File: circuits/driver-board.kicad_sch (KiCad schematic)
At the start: 72 parts, among them J1 Conn_01x18_Female, J2 USB4120-03-C_REVA, J3 Motor_Conn_01x04, J4 Screw_Terminals, J5 Conn_01x06_Female, Q1 SS8050-G, Q2 SS8050-G, SW1 RST_SW_Push, U1 CP2102N-Axx-xQFN24, U2 BA33DD0T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

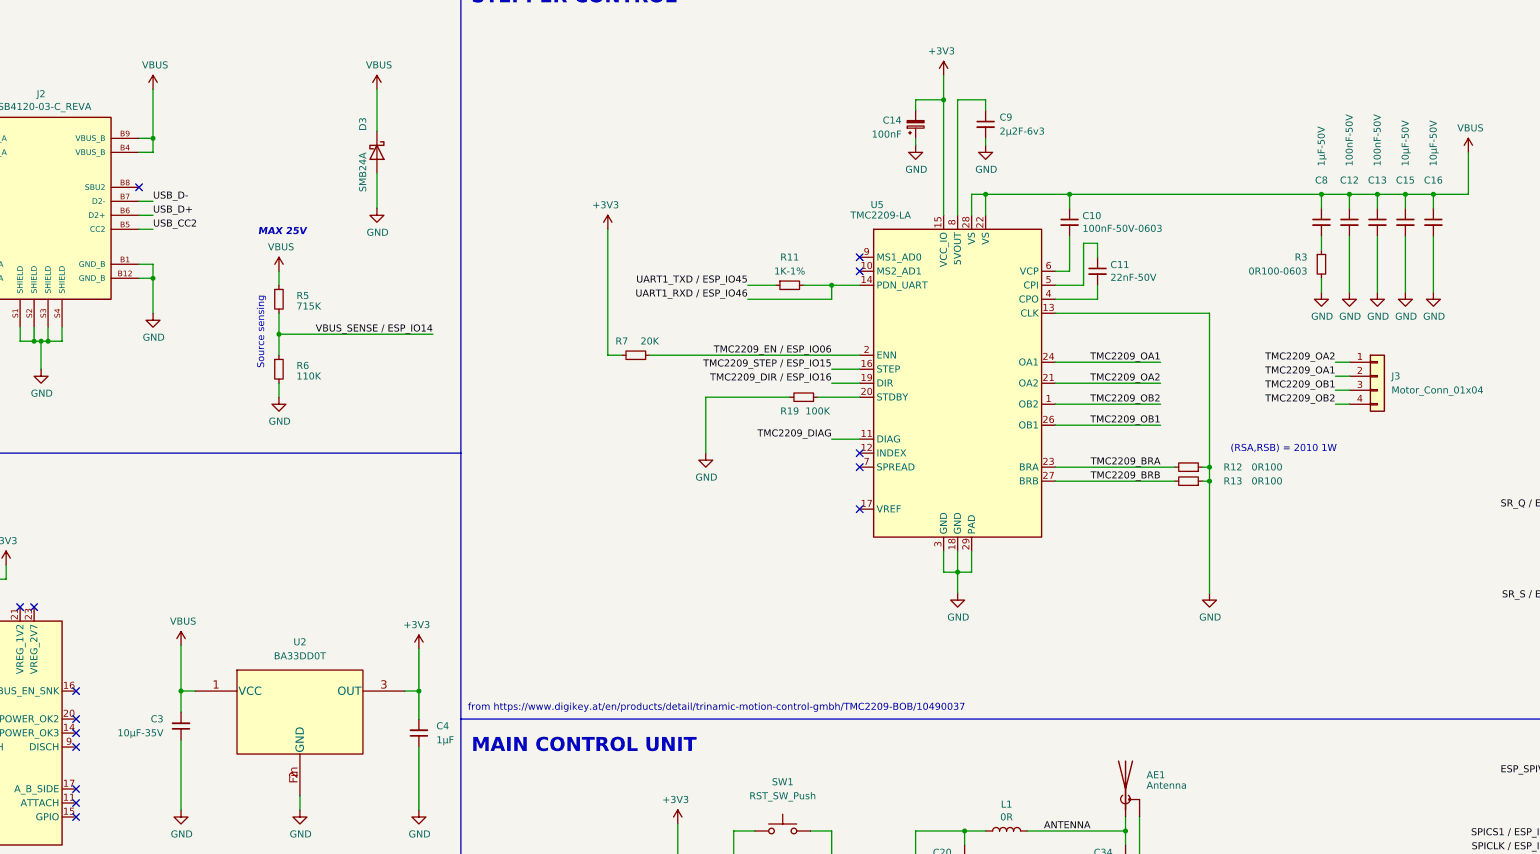
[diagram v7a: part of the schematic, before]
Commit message: gh action and kibot
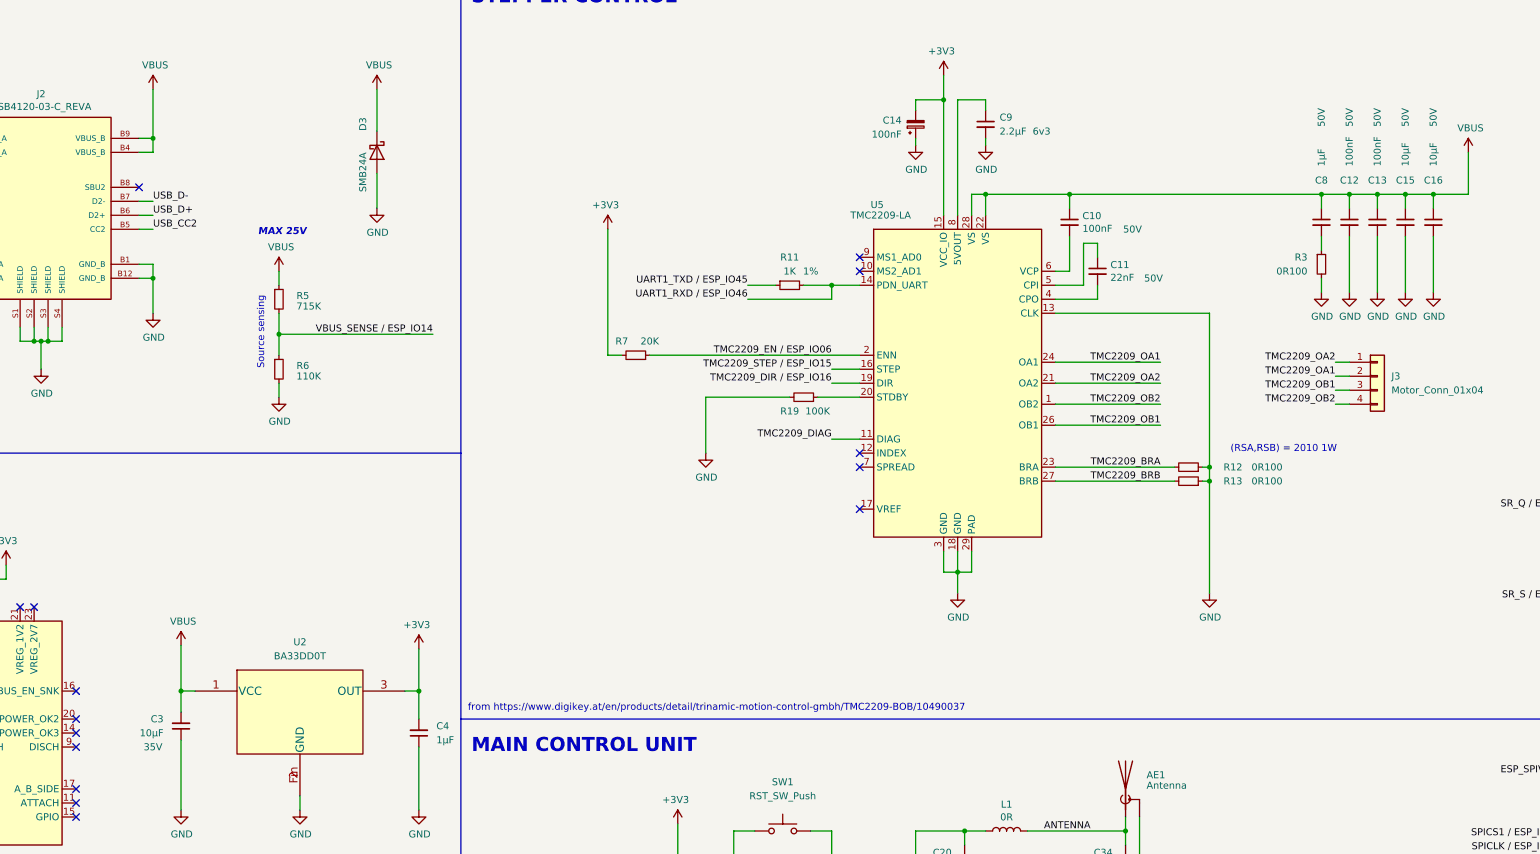
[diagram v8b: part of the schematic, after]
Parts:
- C10: value 100nF-50V-0603 -> 100nF; Voltage (none) -> 50V
- C11: value 22nF-50V -> 22nF; Voltage (none) -> 50V
- C12, C13: value 100nF-50V -> 100nF; Voltage (none) -> 50V
- C15, C16: value 10µF-50V -> 10µF; Voltage (none) -> 50V
- C3: value 10µF-35V -> 10µF; Voltage (none) -> 35V
- C8: value 1µF-50V -> 1µF; Voltage (none) -> 50V
- C9: value 2µ2F-6v3 -> 2.2µF; Voltage (none) -> 6v3
- R11: value 1K-1% -> 1K; Tol (none) -> 1%
- R3: value 0R100-0603 -> 0R100
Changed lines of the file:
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@@
     (in_bom yes) (on_board yes)
     (property "Reference" "R11" (id 0) (at 214.63 68.58 90))
-    (property "Value" "1K-1%" (id 1) (at 214.63 71.12 90))
+    (property "Value" "1K" (id 1) (at 214.63 71.12 90))
     (property "Footprint" "Resistor_SMD:R_0201_0603Metric" (id 2) (at 214.63 73.66 0)
       (effects (font (size 1.27 1.27)) hide)
@@
       (effects (font (size 1.27 1.27)) hide)
     )
+    (property "Tol" "1%" (id 4) (at 218.44 71.12 90))
     (pin "1")
     (pin "2")
@@
       (effects (font (size 1.27 1.27)) (justify left))
     )
-    (property "Value" "2µ2F-6v3" (id 1) (at 252.73 45.72 0)
+    (property "Value" "2.2µF" (id 1) (at 252.73 45.72 0)
       (effects (font (size 1.27 1.27)) (justify left))
     )
@@
       (effects (font (size 1.27 1.27)) hide)
     )
+    (property "Voltage" "6v3" (id 4) (at 260.35 45.72 0))
     (pin "1")
     (pin "2")
@@
       (effects (font (size 1.27 1.27)) (justify left))
     )
-    (property "Value" "22nF-50V" (id 1) (at 272.8468 72.263 0)
+    (property "Value" "22nF" (id 1) (at 272.8468 72.263 0)
       (effects (font (size 1.27 1.27)) (justify left))
     )
@@
       (effects (font (size 1.27 1.27)) hide)
     )
+    (property "Voltage" "50V" (id 4) (at 280.67 72.39 0))
     (pin "1")
     (pin "2")
@@
       (effects (font (size 1.27 1.27)) (justify left))
     )
-    (property "Value" "100nF-50V-0603" (id 1) (at 267.7668 63.373 0)
+    (property "Value" "100nF" (id 1) (at 267.7668 63.373 0)
       (effects (font (size 1.27 1.27)) (justify left))
     )
@@
       (effects (font (size 1.27 1.27)) hide)
     )
+    (property "Voltage" "50V" (id 4) (at 276.86 63.5 0))
     (pin "1")
     (pin "2")
@@
       (effects (font (size 1.27 1.27)) (justify right))
     )
-    (property "Value" "10µF-35V" (id 1) (at 100.965 154.94 0)
+    (property "Value" "10µF" (id 1) (at 100.965 154.94 0)
       (effects (font (size 1.27 1.27)) (justify right))
     )
@@
       (effects (font (size 1.27 1.27)) hide)
     )
+    (property "Voltage" "35V" (id 4) (at 99.06 157.48 0))
     (pin "1")
     (pin "2")
@@
     (in_bom yes) (on_board yes)
     (property "Reference" "C13" (id 0) (at 321.31 54.61 0))
-    (property "Value" "100nF-50V" (id 1) (at 321.31 52.07 90)
+    (property "Value" "100nF" (id 1) (at 321.31 52.07 90)
       (effects (font (size 1.27 1.27)) (justify left))
     )
@@
       (effects (font (size 1.27 1.27)) hide)
     )
+    (property "Voltage" "50V" (id 4) (at 321.31 43.18 90))
     (pin "1")
     (pin "2")
@@
     (in_bom yes) (on_board yes)
     (property "Reference" "C16" (id 0) (at 331.47 54.61 0))
-    (property "Value" "10µF-50V" (id 1) (at 331.47 52.07 90)
+    (property "Value" "10µF" (id 1) (at 331.47 52.07 90)
       (effects (font (size 1.27 1.27)) (justify left))
     )
@@
       (effects (font (size 1.27 1.27)) hide)
     )
+    (property "Voltage" "50V" (id 4) (at 331.47 43.18 90))
     (pin "1")
     (pin "2")
@@
     (in_bom yes) (on_board yes)
     (property "Reference" "C15" (id 0) (at 326.39 54.61 0))
-    (property "Value" "10µF-50V" (id 1) (at 326.39 52.07 90)
+    (property "Value" "10µF" (id 1) (at 326.39 52.07 90)
       (effects (font (size 1.27 1.27)) (justify left))
     )
@@
       (effects (font (size 1.27 1.27)) hide)
     )
+    (property "Voltage" "50V" (id 4) (at 326.39 43.18 90))
     (pin "1")
     (pin "2")
@@
       (effects (font (size 1.27 1.27)) (justify right))
     )
-    (property "Value" "0R100-0603" (id 1) (at 308.61 71.12 0)
+    (property "Value" "0R100" (id 1) (at 308.61 71.12 0)
       (effects (font (size 1.27 1.27)) (justify right))
     )
@@
     (in_bom yes) (on_board yes)
     (property "Reference" "C8" (id 0) (at 311.15 54.61 0))
-    (property "Value" "1µF-50V" (id 1) (at 311.15 52.07 90)
+    (property "Value" "1µF" (id 1) (at 311.15 52.07 90)
       (effects (font (size 1.27 1.27)) (justify left))
     )
@@
       (effects (font (size 1.27 1.27)) hide)
     )
+    (property "Voltage" "50V" (id 4) (at 311.15 43.18 90))
     (pin "1")
     (pin "2")
@@
     (in_bom yes) (on_board yes)
     (property "Reference" "C12" (id 0) (at 316.23 54.61 0))
-    (property "Value" "100nF-50V" (id 1) (at 316.23 52.07 90)
+    (property "Value" "100nF" (id 1) (at 316.23 52.07 90)
       (effects (font (size 1.27 1.27)) (justify left))
     )
@@
       (effects (font (size 1.27 1.27)) hide)
     )
+    (property "Voltage" "50V" (id 4) (at 316.23 43.18 90))
     (pin "1")
     (pin "2")
@@
     )
     (path "/00000000-0000-0000-0000-0000618fda5c"
-      (reference "C3") (unit 1) (value "10µF-35V") (footprint "Capacitor_SMD:C_0402_1005Metric")
+      (reference "C3") (unit 1) (value "10µF") (footprint "Capacitor_SMD:C_0402_1005Metric")
     )
     (path "/00000000-0000-0000-0000-000061aaf580"
@@
     )
     (path "/a9cd33e9-d5e4-4c49-8136-fa738e8ca695"
-      (reference "C8") (unit 1) (value "1µF-50V") (footprint "Capacitor_SMD:C_0603_1608Metric")
+      (reference "C8") (unit 1) (value "1µF") (footprint "Capacitor_SMD:C_0603_1608Metric")
     )
     (path "/00000000-0000-0000-0000-000060b9f380"
-      (reference "C9") (unit 1) (value "2µ2F-6v3") (footprint "Capacitor_SMD:C_0603_1608Metric")
+      (reference "C9") (unit 1) (value "2.2µF") (footprint "Capacitor_SMD:C_0603_1608Metric")
     )
     (path "/00000000-0000-0000-0000-000060fe0dbe"
-      (reference "C10") (unit 1) (value "100nF-50V-0603") (footprint "Capacitor_SMD:C_0603_1608Metric")
+      (reference "C10") (unit 1) (value "100nF") (footprint "Capacitor_SMD:C_0603_1608Metric")
     )
     (path "/00000000-0000-0000-0000-000060fd43a3"
-      (reference "C11") (unit 1) (value "22nF-50V") (footprint "Capacitor_SMD:C_0805_2012Metric")
+      (reference "C11") (unit 1) (value "22nF") (footprint "Capacitor_SMD:C_0805_2012Metric")
     )
     (path "/cb7d9e52-f4b0-4727-ad06-d0e039df1bfd"
-      (reference "C12") (unit 1) (value "100nF-50V") (footprint "Capacitor_SMD:C_0603_1608Metric")
+      (reference "C12") (unit 1) (value "100nF") (footprint "Capacitor_SMD:C_0603_1608Metric")
     )
     (path "/1343b25f-1d1a-4c07-a749-09931c271948"
-      (reference "C13") (unit 1) (value "100nF-50V") (footprint "Capacitor_SMD:C_0603_1608Metric")
+      (reference "C13") (unit 1) (value "100nF") (footprint "Capacitor_SMD:C_0603_1608Metric")
     )
     (path "/99b081e9-e35b-4ab9-ac73-4e355d6f64bd"
@@
     )
     (path "/682aeb00-8195-4c9d-9b9d-6b0f78ccd1d4"
-      (reference "C15") (unit 1) (value "10µF-50V") (footprint "Capacitor_SMD:C_1210_3225Metric")
+      (reference "C15") (unit 1) (value "10µF") (footprint "Capacitor_SMD:C_1210_3225Metric")
     )
     (path "/5581030f-4769-4bf1-b917-f14a09fb1518"
-      (reference "C16") (unit 1) (value "10µF-50V") (footprint "Capacitor_SMD:C_1210_3225Metric")
+      (reference "C16") (unit 1) (value "10µF") (footprint "Capacitor_SMD:C_1210_3225Metric")
     )
     (path "/d3f36edf-27bf-4bf5-9433-1ea4844cdd85"
@@
     )
     (path "/70fef7e4-43a9-4414-8f0d-10a6d2e95116"
-      (reference "R3") (unit 1) (value "0R100-0603") (footprint "Resistor_SMD:R_0603_1608Metric")
+      (reference "R3") (unit 1) (value "0R100") (footprint "Resistor_SMD:R_0603_1608Metric")
     )
     (path "/00000000-0000-0000-0000-000060d89b88"
@@
     )
     (path "/00000000-0000-0000-0000-0000609c62c6"
-      (reference "R11") (unit 1) (value "1K-1%") (footprint "Resistor_SMD:R_0201_0603Metric")
+      (reference "R11") (unit 1) (value "1K") (footprint "Resistor_SMD:R_0201_0603Metric")
     )
     (path "/00000000-0000-0000-0000-000060e012ff"
